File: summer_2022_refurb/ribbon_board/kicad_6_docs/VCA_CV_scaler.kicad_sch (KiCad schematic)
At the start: 4 parts

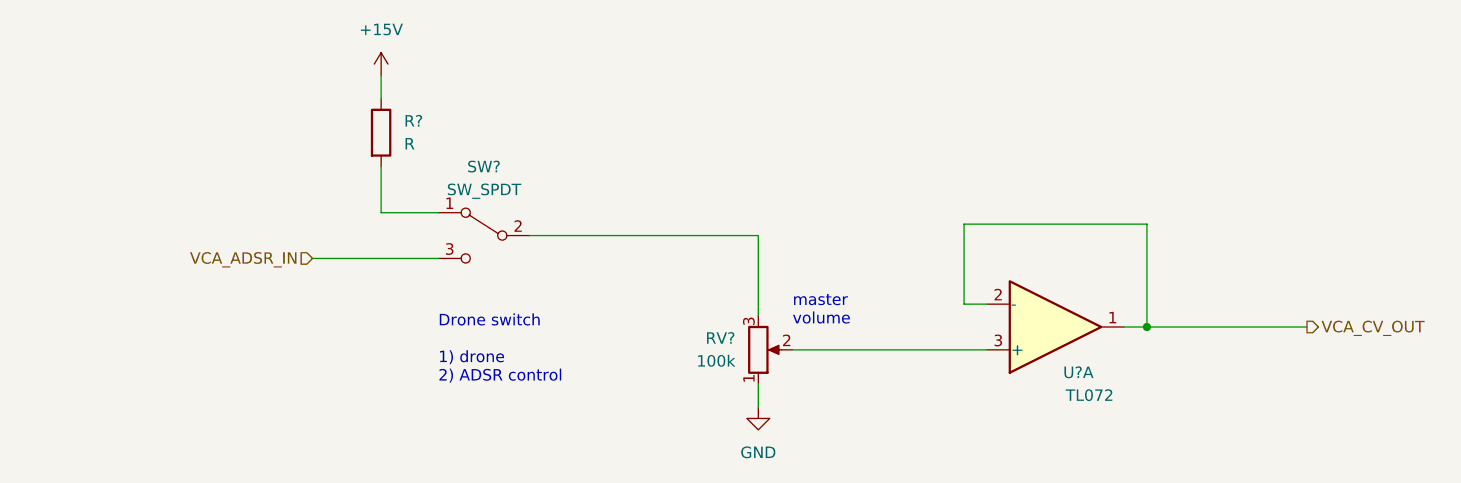
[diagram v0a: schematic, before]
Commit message: Progress on ribbon board
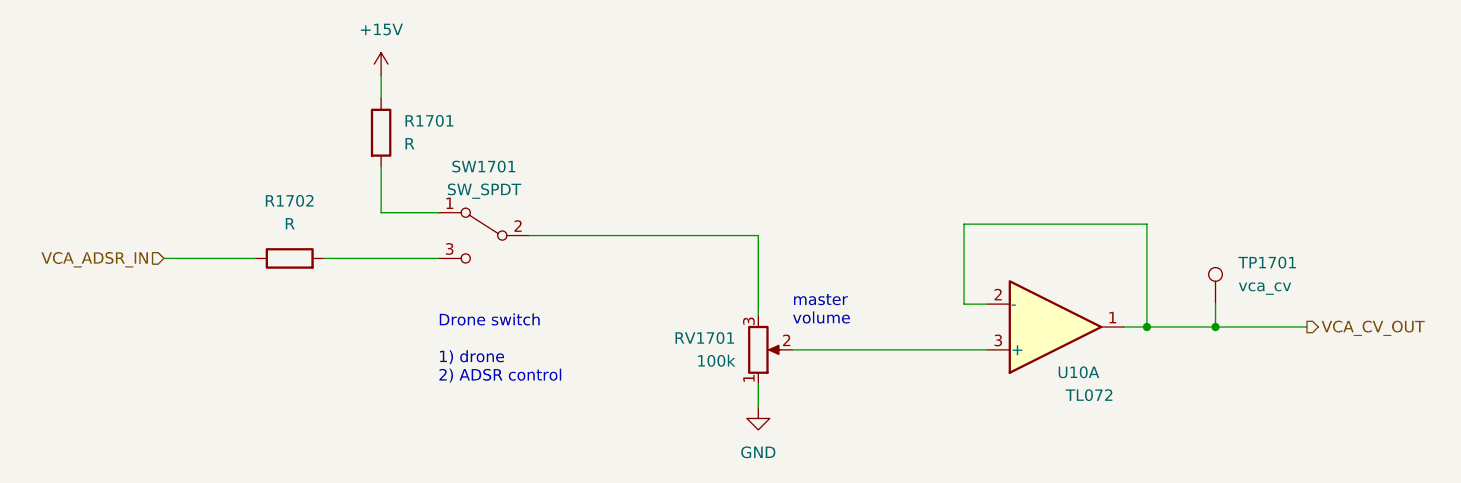
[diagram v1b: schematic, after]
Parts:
- added R1702: R, Resistor_SMD:R_0805_2012Metric, symbol Device:R
- added TP1701: vca_cv, TestPoint:TestPoint_Keystone_5000-5004_Miniature, symbol Connector:TestPoint
- R1701: renamed from R?; footprint (none) -> Resistor_SMD:R_0805_2012Metric
- RV1701: renamed from RV?; footprint (none) -> Potentiometer_THT:Potentiometer_Alpha_RD901F-40-00D_Single_Vertical
- SW1701: renamed from SW?; footprint (none) -> custom_footprints:SPDT_mini_toggle
- U10: renamed from U?; footprint (none) -> Package_SO:SO-8_5.3x6.2mm_P1.27mm
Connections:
- net VCA_ADSR_IN: now also R1702.1; no longer SW1701.3 (C)
- net VCA_CV_OUT: now also TP1701.1
- new net: R1702.2, SW1701.3 (C)
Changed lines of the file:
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@@
   (title_block
     (title "Josh Ox Ribbon Synth Ribbon board")
-    (date "2022-06-16")
+    (date "2022-06-17")
     (rev "0")
     (comment 1 "creativecommons.org/licences/by/4.0")
@@
   (junction (at 189.23 101.6) (diameter 0) (color 0 0 0 0)
   )
-  (wire (pts (xy 96.52 93.98) (xy 110.49 93.98))
+  (junction (at 196.85 101.6) (diameter 0) (color 0 0 0 0)
+  )
+  (wire (pts (xy 80.01 93.98) (xy 90.17 93.98))
     (stroke (width 0) (type default) (color 0 0 0 0))
   )
@@
     (stroke (width 0) (type default) (color 0 0 0 0))
   )
+  (wire (pts (xy 196.85 101.6) (xy 207.01 101.6))
+    (stroke (width 0) (type default) (color 0 0 0 0))
+  )
   (wire (pts (xy 168.91 90.17) (xy 189.23 90.17))
     (stroke (width 0) (type default) (color 0 0 0 0))
   )
-  (wire (pts (xy 189.23 101.6) (xy 207.01 101.6))
+  (wire (pts (xy 189.23 101.6) (xy 196.85 101.6))
     (stroke (width 0) (type default) (color 0 0 0 0))
   )
   (wire (pts (xy 168.91 99.06) (xy 168.91 90.17))
+    (stroke (width 0) (type default) (color 0 0 0 0))
+  )
+  (wire (pts (xy 97.79 93.98) (xy 110.49 93.98))
+    (stroke (width 0) (type default) (color 0 0 0 0))
+  )
+  (wire (pts (xy 196.85 99.06) (xy 196.85 101.6))
     (stroke (width 0) (type default) (color 0 0 0 0))
   )
@@
     (effects (font (size 1.27 1.27)) (justify left bottom))
   )
-  (hierarchical_label "VCA_ADSR_IN" (shape input) (at 96.52 93.98 180)
+  (hierarchical_label "VCA_ADSR_IN" (shape input) (at 80.01 93.98 180)
     (effects (font (size 1.27 1.27)) (justify right))
   )
@@
   (symbol (lib_id "Device:R") (at 104.14 80.01 0) (unit 1)
     (in_bom yes) (on_board yes) (fields_autoplaced)
-    (property "Reference" "R?" (id 0) (at 106.68 78.7399 0)
+    (property "Reference" "R1701" (id 0) (at 106.68 78.7399 0)
       (effects (font (size 1.27 1.27)) (justify left))
     )
@@
       (effects (font (size 1.27 1.27)) (justify left))
     )
-    (property "Footprint" "" (id 2) (at 102.362 80.01 90)
+    (property "Footprint" "Resistor_SMD:R_0805_2012Metric" (id 2) (at 102.362 80.01 90)
       (effects (font (size 1.27 1.27)) hide)
     )
@@
   (symbol (lib_id "power:GND") (at 146.05 110.49 0) (unit 1)
     (in_bom yes) (on_board yes) (fields_autoplaced)
-    (property "Reference" "#PWR?" (id 0) (at 146.05 116.84 0)
+    (property "Reference" "#PWR01702" (id 0) (at 146.05 116.84 0)
       (effects (font (size 1.27 1.27)) hide)
     )
@@
     (pin "1")
   )
+  (symbol (lib_id "Connector:TestPoint") (at 196.85 99.06 0) (unit 1)
+    (in_bom no) (on_board yes) (fields_autoplaced)
+    (property "Reference" "TP1701" (id 0) (at 199.39 94.4879 0)
+      (effects (font (size 1.27 1.27)) (justify left))
+    )
+    (property "Value" "vca_cv" (id 1) (at 199.39 97.0279 0)
+      (effects (font (size 1.27 1.27)) (justify left))
+    )
+    (property "Footprint" "TestPoint:TestPoint_Keystone_5000-5004_Miniature" (id 2) (at 201.93 99.06 0)
+      (effects (font (size 1.27 1.27)) hide)
+    )
+    (property "Datasheet" "~" (id 3) (at 201.93 99.06 0)
+      (effects (font (size 1.27 1.27)) hide)
+    )
+    (pin "1")
+  )
   (symbol (lib_id "Amplifier_Operational:TL072") (at 179.07 101.6 0) (mirror x) (unit 1)
     (in_bom yes) (on_board yes)
-    (property "Reference" "U?" (id 0) (at 181.61 106.68 0))
+    (property "Reference" "U10" (id 0) (at 181.61 106.68 0))
     (property "Value" "TL072" (id 1) (at 182.88 109.22 0))
-    (property "Footprint" "" (id 2) (at 179.07 101.6 0)
+    (property "Footprint" "Package_SO:SO-8_5.3x6.2mm_P1.27mm" (id 2) (at 179.07 101.6 0)
       (effects (font (size 1.27 1.27)) hide)
     )
@@
     (pin "8")
   )
+  (symbol (lib_id "Device:R") (at 93.98 93.98 90) (unit 1)
+    (in_bom yes) (on_board yes) (fields_autoplaced)
+    (property "Reference" "R1702" (id 0) (at 93.98 87.63 90))
+    (property "Value" "R" (id 1) (at 93.98 90.17 90))
+    (property "Footprint" "Resistor_SMD:R_0805_2012Metric" (id 2) (at 93.98 95.758 90)
+      (effects (font (size 1.27 1.27)) hide)
+    )
+    (property "Datasheet" "~" (id 3) (at 93.98 93.98 0)
+      (effects (font (size 1.27 1.27)) hide)
+    )
+    (pin "1")
+    (pin "2")
+  )
   (symbol (lib_id "power:+15V") (at 104.14 73.66 0) (unit 1)
     (in_bom yes) (on_board yes) (fields_autoplaced)
-    (property "Reference" "#PWR?" (id 0) (at 104.14 77.47 0)
+    (property "Reference" "#PWR01701" (id 0) (at 104.14 77.47 0)
       (effects (font (size 1.27 1.27)) hide)
     )
@@
   (symbol (lib_id "Switch:SW_SPDT") (at 115.57 91.44 0) (mirror y) (unit 1)
     (in_bom yes) (on_board yes) (fields_autoplaced)
-    (property "Reference" "SW?" (id 0) (at 115.57 83.82 0))
+    (property "Reference" "SW1701" (id 0) (at 115.57 83.82 0))
     (property "Value" "SW_SPDT" (id 1) (at 115.57 86.36 0))
-    (property "Footprint" "" (id 2) (at 115.57 91.44 0)
+    (property "Footprint" "custom_footprints:SPDT_mini_toggle" (id 2) (at 115.57 91.44 0)
       (effects (font (size 1.27 1.27)) hide)
     )
@@
   (symbol (lib_id "Device:R_Potentiometer") (at 146.05 104.14 0) (mirror x) (unit 1)
     (in_bom yes) (on_board yes) (fields_autoplaced)
-    (property "Reference" "RV?" (id 0) (at 143.51 102.8699 0)
+    (property "Reference" "RV1701" (id 0) (at 143.51 102.8699 0)
       (effects (font (size 1.27 1.27)) (justify right))
     )
@@
       (effects (font (size 1.27 1.27)) (justify right))
     )
-    (property "Footprint" "" (id 2) (at 146.05 104.14 0)
+    (property "Footprint" "Potentiometer_THT:Potentiometer_Alpha_RD901F-40-00D_Single_Vertical" (id 2) (at 146.05 104.14 0)
       (effects (font (size 1.27 1.27)) hide)
     )
